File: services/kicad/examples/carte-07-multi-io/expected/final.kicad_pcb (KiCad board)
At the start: 2 copper layers, 110 x 80 mm, 44 parts, among them J1 IN_5V, J2 SWD, J3 IO0, J4 IO1, J5 IO2, U1 STM32F103C8T6, U2 AMS1117-3.3

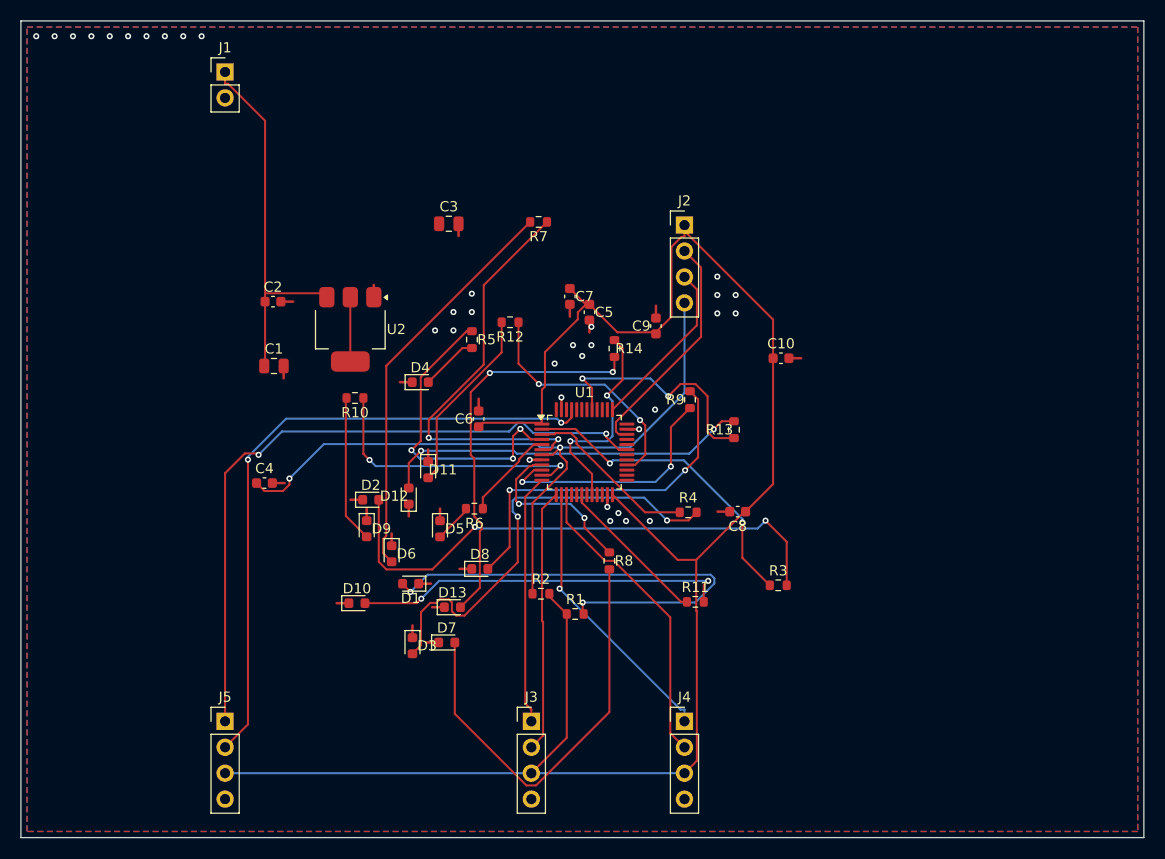
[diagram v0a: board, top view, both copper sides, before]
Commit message: test(examples): carte 07 rejouee -- la preuve bout en bout des trois correctifs
Les correctifs du commit precedent etaient mesures ISOLEMENT : la grille sur un
board place, les nets sur les onze boards versionnes. Aucune carte n etait
ressortie complete de la chaine avec eux. C est fait.

                        grille        paires             pastilles perdues
    AVANT   carte-07     2/44   5 %   23,8 mm (max 41)   4  dont U2.2
    APRES   carte-07    37/44  84 %   15,7 mm (max 33)   0

Board livre : **100 % route, DRC clean, 20 fichiers exportes**. Les 118
violations restantes sont TOUTES de la serigraphie (`silk_over_copper:82`,
`silk_overlap:36`) — verifie par un DRC complet : **0 erreur**.

`U2.2`, la sortie du regulateur AMS1117-3.3 que la capture de l utilisateur
montrait sur `Net-(U2-2)`, porte desormais `+3V3`. Les trois autres pastilles
d alimentation perdues aussi.

⚠️ Sur la grille, la carte DEPASSE maintenant la reference humaine : 84 % contre
65 % sur `astra_piNas`. Sur les paires, elle reste derriere : 15,7 mm contre
9,8 mm. Le serrage est ameliore de 34 %, pas resolu — la moitie des paires reste
bloquee par les attaches insatisfiables (decision `D-2026-09-08-c`, en attente).

LE BOARD PLACE EST LIVRE AVEC

`expected/placement.kicad_pcb` rejoint `final.kicad_pcb`. Demande explicite de
l utilisateur : « je veux toujours voir le fichier placement et routage ». Et
c est surtout le TEMOIN : sans lui, on impute au routage des defauts qui
preexistaient — faute deja commise dans ce depot, 204 erreurs DRC attribuees au
routeur sur un board sans la moindre piste.

⚠️ CINQ EXECUTIONS PERDUES AVANT CELLE-CI, et la cause n etait pas la memoire.
Chaque mise a mort cote Windows laissait son pipeline VIVANT dans le conteneur :
quatre orphelins accumules, deux encore actifs a 380 % de CPU vingt minutes plus
tard. Ils consommaient la memoire qui faisait tuer la suivante — une spirale que
chaque relance alimentait. La sixieme a ete lancee DETACHEE dans le conteneur
(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
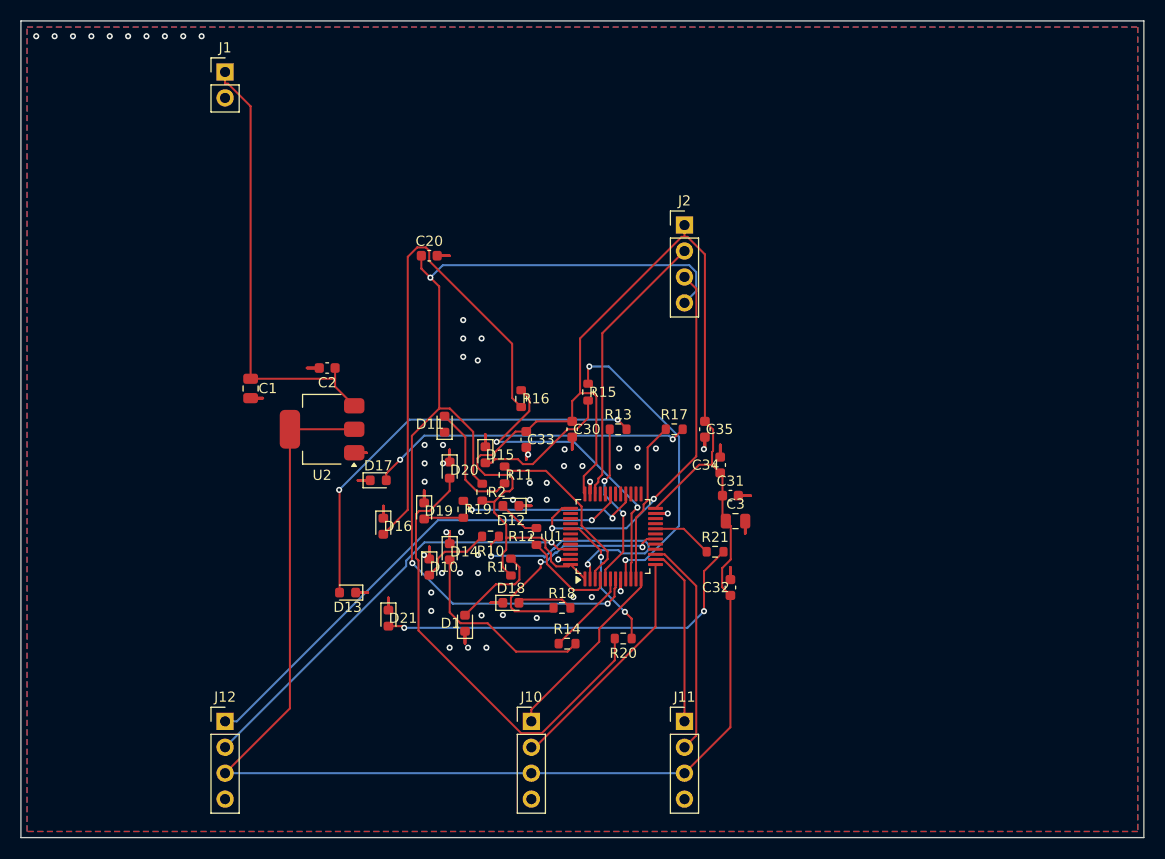
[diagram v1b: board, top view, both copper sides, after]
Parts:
- removed C10, C4, C5, C6, C7, C8, C9: 100nF, C_0603_1608Metric
- removed D2, D3, D4, D5, D6, D7, D8, D9: LED, LED_0603_1608Metric
- removed J3: IO0, PinHeader_1x04_P2.54mm_Vertical
- removed J4: IO1, PinHeader_1x04_P2.54mm_Vertical
- removed J5: IO2, PinHeader_1x04_P2.54mm_Vertical
- removed R3, R4, R5, R6, R7, R8, R9: 1k, R_0603_1608Metric
- added C20: 100nF, C_0603_1608Metric, F.Cu at (133.5, 88.0)
- added C30: 100nF, C_0603_1608Metric, F.Cu at (147.5, 105.0)
- added C31: 100nF, C_0603_1608Metric, F.Cu at (163.0, 111.5)
- added C32: 100nF, C_0603_1608Metric, F.Cu at (163.0, 120.5)
- added C33: 100nF, C_0603_1608Metric, F.Cu at (143.0, 106.0)
- added C34: 100nF, C_0603_1608Metric, F.Cu at (162.0, 108.5)
- added C35: 100nF, C_0603_1608Metric, F.Cu at (160.5, 105.0)
- added D14: LED, LED_0603_1608Metric, F.Cu at (135.5, 117.0)
- added D15: LED, LED_0603_1608Metric, F.Cu at (139.0, 107.5)
- added D16: LED, LED_0603_1608Metric, F.Cu at (129.0, 114.5)
- added D17: LED, LED_0603_1608Metric, F.Cu at (128.5, 110.0)
- added D18: LED, LED_0603_1608Metric, F.Cu at (141.5, 122.0)
- added D19: LED, LED_0603_1608Metric, F.Cu at (133.0, 113.0)
- added D20: LED, LED_0603_1608Metric, F.Cu at (135.5, 109.0)
- added D21: LED, LED_0603_1608Metric, F.Cu at (129.5, 123.5)
- added J10: IO0, PinHeader_1x04_P2.54mm_Vertical, F.Cu at (143.5, 133.6)
- added J11: IO1, PinHeader_1x04_P2.54mm_Vertical, F.Cu at (158.5, 133.6)
- added J12: IO2, PinHeader_1x04_P2.54mm_Vertical, F.Cu at (113.5, 133.6)
- added R15: 1k, R_0603_1608Metric, F.Cu at (149.1, 101.4)
- added R16: 1k, R_0603_1608Metric, F.Cu at (142.5, 102.0)
- added R17: 1k, R_0603_1608Metric, F.Cu at (157.5, 105.0)
- added R18: 1k, R_0603_1608Metric, F.Cu at (146.5, 122.5)
- added R19: 1k, R_0603_1608Metric, F.Cu at (136.8, 112.8)
- added R20: 1k, R_0603_1608Metric, F.Cu at (152.5, 125.5)
- added R21: 1k, R_0603_1608Metric, F.Cu at (161.5, 117.0)
- moved C3 40.5 mm to (163.5, 114.0)
- moved R14 29.3 mm to (147.0, 126.0), turned to 0 degrees
- moved R11 22.4 mm to (140.9, 109.5), turned to -90 degrees
- moved R12 21.1 mm to (144.0, 115.5), turned to 90 degrees
- moved R10 19.0 mm to (139.5, 115.5)
- moved R2 11.5 mm to (138.7, 111.2), turned to -90 degrees
- moved R13 11.3 mm to (152.0, 105.0), turned to 0 degrees
- moved D13 10.4 mm to (125.5, 121.0), turned to 180 degrees
- moved U2 10.2 mm to (123.0, 105.0), turned to 180 degrees
- moved D12 10.1 mm to (141.5, 112.5), turned to 180 degrees
- moved U1 8.72 mm to (151.5, 115.5), turned to 90 degrees
- moved C2 8.39 mm to (123.5, 99.0), turned to 180 degrees
- moved D10 7.92 mm to (133.5, 118.5), turned to -90 degrees
- moved R1 7.79 mm to (141.5, 118.5), turned to 90 degrees
- moved D1 6.59 mm to (137.0, 124.0), turned to 90 degrees
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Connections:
- C3 pad 1: Net-(C3-1) -> +3V3
- D10 pad 2: LEDA8 -> LEDA0
- D11 pad 2: LEDA9 -> LEDA1
- D12 pad 2: LEDA10 -> LEDA2
- D13 pad 2: LEDA11 -> LEDA3
- R10 pad 1: IO_L7 -> IO_L0
- R10 pad 2: LEDA7 -> LEDA0
- R11 pad 1: IO_L8 -> IO_L1
- R11 pad 2: LEDA8 -> LEDA1
- R12 pad 1: IO_L9 -> IO_L2
- R12 pad 2: LEDA9 -> LEDA2
- R13 pad 1: IO_L10 -> IO_L3
- R13 pad 2: LEDA10 -> LEDA3
- R14 pad 1: IO_L11 -> IO_L4
- R14 pad 2: LEDA11 -> LEDA4
- U1 pad 36: Net-(U1-36) -> +3V3
- U1 pad 48: Net-(U1-48) -> +3V3
- U2 pad 2: Net-(U2-2) -> +3V3
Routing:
- net GND: track 33.6 -> 97.2 mm, vias 34 -> 56
- net +3V3: track 178.1 -> 226.6 mm
- net LEDA0: track 53.6 -> 7.20 mm, vias 2 -> 0
- net LED_PWR: track 47.1 -> 9.18 mm, vias 2 -> 0
- net LEDA3: track 3.82 -> 41.5 mm, vias 0 -> 2
- net IO_L4: track 40.9 -> 8.44 mm, vias 2 -> 0
- net LEDA1: track 43.4 -> 11.7 mm, vias 2 -> 0
- net LEDA8: track 36.8 -> 5.51 mm, vias 2 -> 0
- net LEDA5: track 42.0 -> 14.0 mm
- net NRST: track 73.7 -> 95.5 mm, vias 2 -> 3
- net SWCLK: track 16.9 -> 38.4 mm, vias 0 -> 2
- net IO_L2: track 30.7 -> 9.50 mm, vias 3 -> 0
- net EXT2_2: track 63.8 -> 42.7 mm, vias 2 -> 1
- net LEDA4: track 39.6 -> 19.4 mm
- net EXT2_1: track 67.1 -> 47.5 mm, vias 2 -> 1
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
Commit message: feat(examples): carte-07 livree -- 100 %, 0 erreur, 2 couches, decouplage 2,5 mm, paires 2,5 mm, grille 91 %
Placement complet (contrainte de decouplage + rangees LED/R + une capa par broche VDD), tirage de preuve sous le plancher. Placement livre a cote du board route.

Co-Authored-By: Claude Fable 5.1 <noreply@anthropic.com>

Claude-Session: https://claude.ai/code/session_01TnMqm4La2CxQHHB5K8aSSV
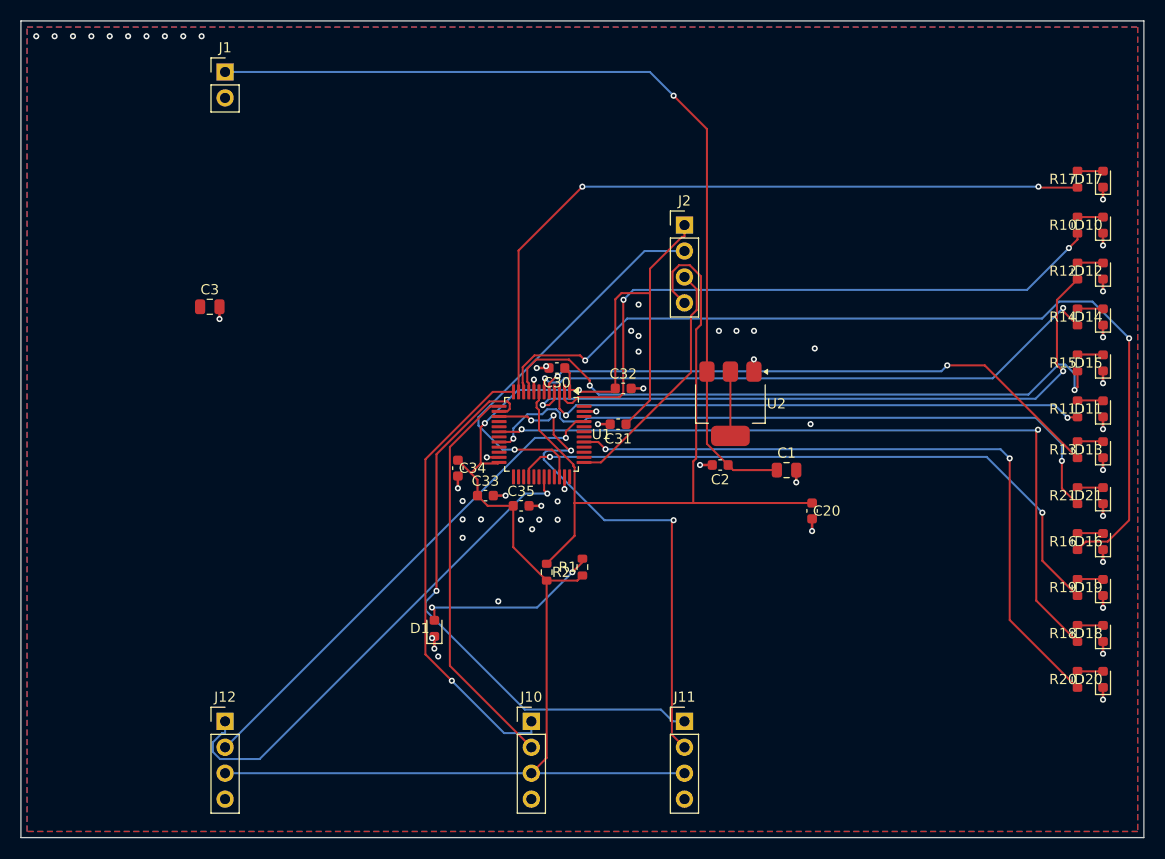
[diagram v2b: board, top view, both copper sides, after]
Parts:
- moved D17 76.9 mm to (199.5, 80.5), turned to 90 degrees
- moved D13 75.3 mm to (199.5, 107.0), turned to 90 degrees
- moved D10 74.0 mm to (199.5, 85.0), turned to 90 degrees
- moved D21 71.0 mm to (199.5, 111.5), turned to 90 degrees
- moved D16 70.5 mm to (199.5, 116.0), turned to 90 degrees
- moved D14 68.0 mm to (199.5, 94.0), turned to 90 degrees
- moved D20 67.2 mm to (199.5, 129.5), turned to 90 degrees
- moved D19 66.9 mm to (199.5, 120.5), turned to 90 degrees
- moved R10 65.1 mm to (197.0, 85.0), turned to 90 degrees
- moved D11 64.5 mm to (199.5, 103.0)
- moved D12 62.4 mm to (199.5, 89.5), turned to 90 degrees
- moved D15 61.2 mm to (199.5, 98.5), turned to 90 degrees
- moved R19 60.6 mm to (197.0, 120.5), turned to 90 degrees
- moved R14 59.4 mm to (197.0, 94.0), turned to 90 degrees
- moved R12 59.0 mm to (197.0, 89.5)
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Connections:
- C3 pad 1: +3V3 -> Net-(C3-1)
- U1 pad 36: +3V3 -> Net-(U1-36)
- U1 pad 48: +3V3 -> Net-(U1-48)
- U2 pad 2: +3V3 -> Net-(U2-2)
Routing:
- net +3V3: track 226.6 -> 144.5 mm, vias 0 -> 2
- net GND: track 97.2 -> 33.6 mm, vias 56 -> 60
- net IO_L6: track 30.7 -> 90.5 mm
- net IO_L11: track 5.94 -> 65.6 mm, vias 0 -> 2
- net IO_L7: track 15.9 -> 71.2 mm, vias 0 -> 2
- net IO_L2: track 9.50 -> 64.6 mm, vias 0 -> 2
- net IO_L10: track 13.7 -> 67.6 mm
- net IO_L8: track 22.6 -> 75.5 mm
- net IO_L4: track 8.44 -> 57.6 mm, vias 0 -> 2
- net LEDA6: track 49.8 -> 2.52 mm
- net IO_L9: track 18.3 -> 63.4 mm
- net VIN: track 44.0 -> 88.3 mm, vias 0 -> 1
- net LEDA10: track 45.5 -> 2.52 mm
- net IO_L3: track 16.4 -> 57.1 mm
- net EXT1_1: track 17.5 -> 56.6 mm, vias 0 -> 1
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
